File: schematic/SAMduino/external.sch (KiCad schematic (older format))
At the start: 16 parts, among them IC4 SST26VF064B-104V_SM, IC5 MCP2221-I_SL, IC6 MCP2542FD-E_SN, J5 Conn_01x02, J6 Conn_01x02

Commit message: Specialty pins wired
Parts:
- removed JP1: SolderJumper_2_Bridged, symbol Jumper:SolderJumper_2_Bridged
- added R?: 100k, symbol Device:R
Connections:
- net labels added: NRST, QCS, QIO0, QIO1, QIO2, QIO3, QSCK, URXD0, UTXD0
- net labels removed: MCLR, U2RX, U2TX
- wire segments 50 -> 57
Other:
- moved on the sheet: C24
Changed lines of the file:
@@
 	4800 4500 4050 4500
 Text GLabel 1800 4600 0    50   Input ~ 0
-MCLR
+NRST
 Text GLabel 1800 4700 0    50   Input ~ 0
-U2RX
+URXD0
 Text GLabel 1800 4800 0    50   Input ~ 0
-U2TX
+UTXD0
 Wire Wire Line
 	1800 4700 2950 4700
@@
 L power:GND #PWR028
 U 1 1 616BDAE8
-P 3600 1600
-F 0 "#PWR028" H 3600 1350 50  0001 C CNN
-F 1 "GND" H 3605 1427 50  0000 C CNN
-F 2 "" H 3600 1600 50  0001 C CNN
-F 3 "" H 3600 1600 50  0001 C CNN
-	1    3600 1600
+P 3800 1600
+F 0 "#PWR028" H 3800 1350 50  0001 C CNN
+F 1 "GND" H 3805 1427 50  0000 C CNN
+F 2 "" H 3800 1600 50  0001 C CNN
+F 3 "" H 3800 1600 50  0001 C CNN
+	1    3800 1600
 	1    0    0    -1
 $EndComp
@@
 L Device:C C24
 U 1 1 616BE1BB
-P 3300 1600
-F 0 "C24" H 3415 1646 50  0000 L CNN
-F 1 "100n" H 3415 1555 50  0000 L CNN
-F 2 "" H 3338 1450 50  0001 C CNN
-F 3 "~" H 3300 1600 50  0001 C CNN
-	1    3300 1600
+P 3500 1600
+F 0 "C24" V 3250 1500 50  0000 L CNN
+F 1 "100n" V 3350 1500 50  0000 L CNN
+F 2 "" H 3538 1450 50  0001 C CNN
+F 3 "~" H 3500 1600 50  0001 C CNN
+	1    3500 1600
 	0    1    1    0
 $EndComp
 Text GLabel 3000 1300 1    50   Input ~ 0
 VCC3V3
-$Comp
-L Jumper:SolderJumper_2_Bridged JP1
-U 1 1 616C3578
-P 2000 4600
-F 0 "JP1" H 2000 4713 50  0000 C CNN
-F 1 "SolderJumper_2_Bridged" H 2000 4714 50  0001 C CNN
-F 2 "" H 2000 4600 50  0001 C CNN
-F 3 "~" H 2000 4600 50  0001 C CNN
-	1    2000 4600
-	1    0    0    -1
-$EndComp
-Wire Wire Line
-	2150 4600 2950 4600
-Wire Wire Line
-	1850 4600 1800 4600
 Text Notes 7900 3000 0    50   ~ 0
 CAN Transceiver
@@
 	2900 1600 3000 1600
 Wire Wire Line
-	3450 1600 3600 1600
+	3650 1600 3800 1600
 Wire Wire Line
 	3000 1300 3000 1600
+Text GLabel 3050 1800 2    50   Input ~ 0
+QSCK
+Text GLabel 3050 1900 2    50   Input ~ 0
+QIO0
+Text GLabel 1150 1700 0    50   Input ~ 0
+QIO1
+Text GLabel 1150 1800 0    50   Input ~ 0
+QIO2
+Text GLabel 3050 1700 2    50   Input ~ 0
+QIO3
+Text GLabel 1150 1600 0    50   Input ~ 0
+QCS
+Wire Wire Line
+	3000 1600 3350 1600
 Connection ~ 3000 1600
 Wire Wire Line
-	3000 1600 3150 1600
+	3050 1700 2900 1700
+Wire Wire Line
+	3050 1800 2900 1800
+Wire Wire Line
+	3050 1900 2900 1900
+Wire Wire Line
+	1150 1800 1300 1800
+Wire Wire Line
+	1150 1700 1300 1700
+Wire Wire Line
+	1150 1600 1300 1600
+$Comp
+L Device:R R?
+U 1 1 6163C603
+P 1300 1250
+F 0 "R?" H 1370 1296 50  0000 L CNN
+F 1 "100k" H 1370 1205 50  0000 L CNN
+F 2 "" V 1230 1250 50  0001 C CNN
+F 3 "~" H 1300 1250 50  0001 C CNN
+	1    1300 1250
+	1    0    0    -1
+$EndComp
+Text GLabel 1300 1000 1    50   Input ~ 0
+VCC3V3
+Wire Wire Line
+	1300 1400 1300 1600
+Connection ~ 1300 1600
+Wire Wire Line
+	1300 1100 1300 1000
+Wire Wire Line
+	1800 4600 2950 4600
 $EndSCHEMATC

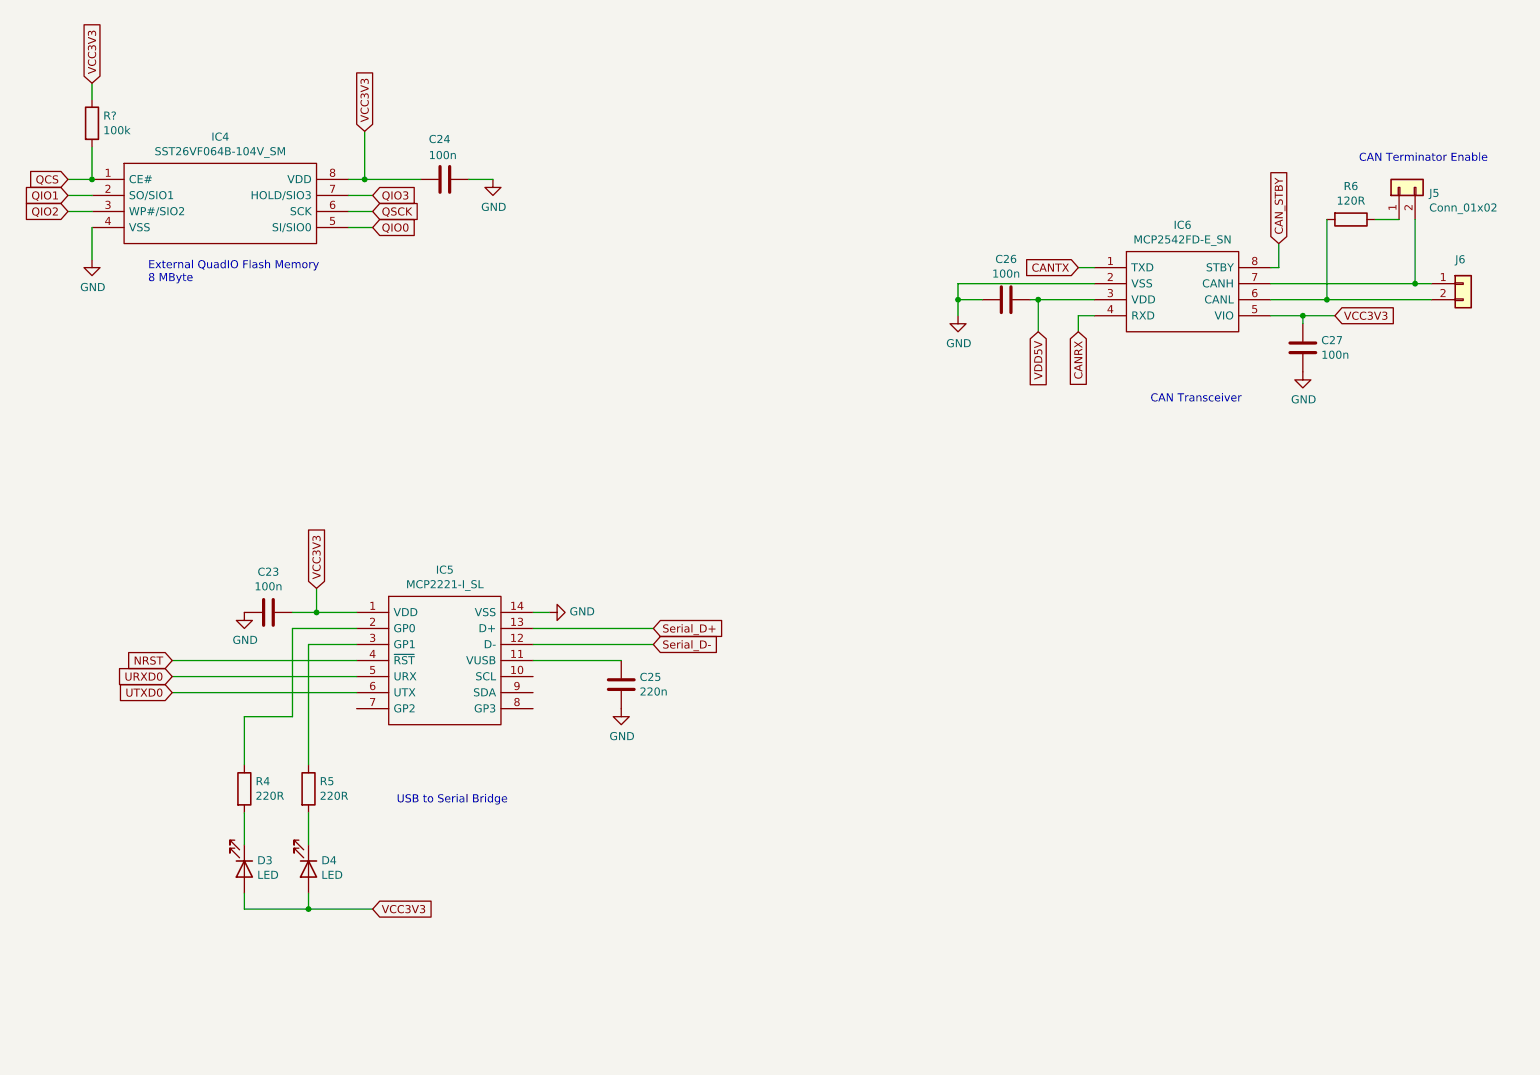
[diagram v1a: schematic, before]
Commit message: All pins connected
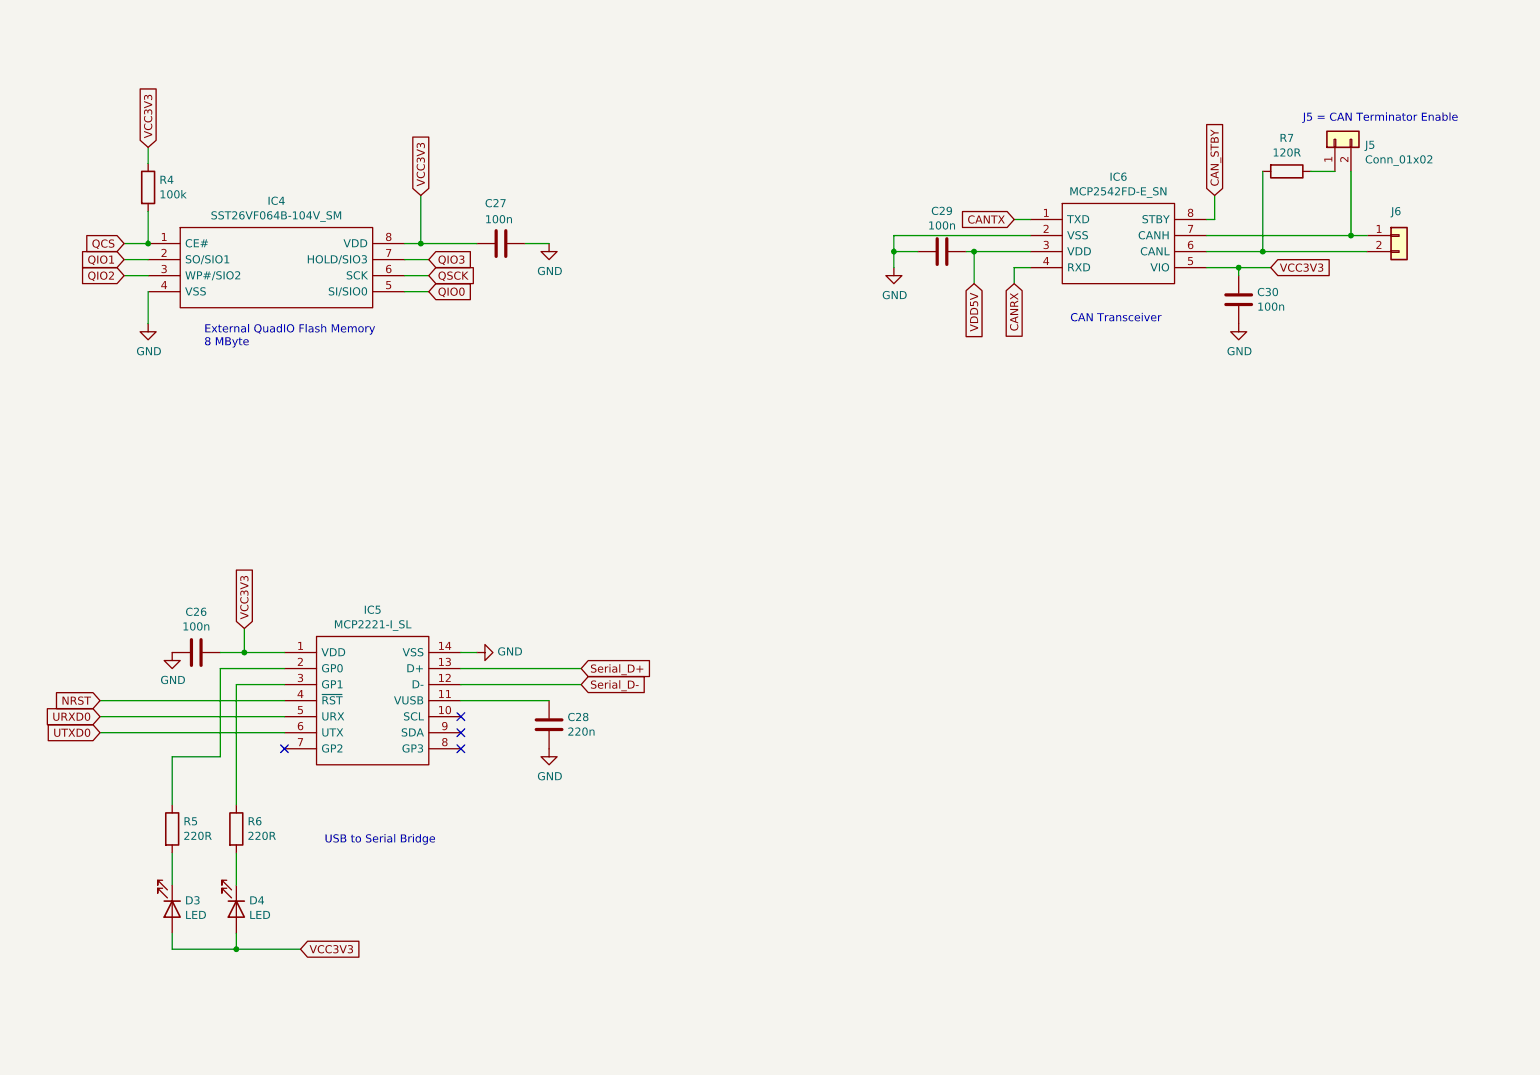
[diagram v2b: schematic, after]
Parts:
- gave numbers to parts that had none: 1
- renumbered C23 to C26, C24 to C27, C25 to C28, C26 to C29, C27 to C30, R4 to R5, R5 to R6, R6 to R7
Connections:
- no-connect marks 0 -> 4
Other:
- note added: "J5 = CAN Terminator Enable"
- note removed: "CAN Terminator Enable"
- moved on the sheet: C26, C27, C28, C29, C30, D3, D4, IC4, IC5, IC6, J5, J6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

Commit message: Schematic with footprints
Some footprints need to be verified with actual components
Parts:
- removed J6: Conn_01x02, symbol Connector_Generic:Conn_01x02
- added J6: Screw_Terminal_01x02, SamacSys_Parts:1725656, symbol Connector:Screw_Terminal_01x02
- C26, C27, C28, C29, C30: footprint (none) -> Capacitor_SMD:C_0603_1608Metric
- D3: value LED -> Green; footprint (none) -> LED_SMD:LED_0603_1608Metric
- D4: value LED -> Yellow; footprint (none) -> LED_SMD:LED_0603_1608Metric
- IC4: footprint SOIC127P794X203-8N -> SamacSys_Parts:SOIC127P794X203-8N
- IC5: footprint SOIC127P600X175-14N -> SamacSys_Parts:SOIC127P600X175-14N
- IC6: footprint SOIC127P600X175-8N -> SamacSys_Parts:SOIC127P600X175-8N
- J5: footprint (none) -> Connector_PinHeader_2.54mm:PinHeader_1x02_P2.54mm_Vertical
- R4, R5, R6: footprint (none) -> Resistor_SMD:R_0603_1608Metric
- R7: footprint (none) -> Resistor_SMD:R_0805_2012Metric
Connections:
- net URXD0: now also IC5.6 (UTX); no longer IC5.5 (URX)
- net UTXD0: now also IC5.5 (URX); no longer IC5.6 (UTX)
- net VCC3V3: now also C28.1, IC5.11 (VUSB)
- net at IC6.6 (CANL), R7.2: now also J6.2 (Pin_2)
- net at IC6.7 (CANH), J5.2 (Pin_2): now also J6.1 (Pin_1)
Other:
- note added: "Is this needed? or 100n instead?"
- note added: "MCU Rx\nindicator"
- note added: "MCU Tx\nindicator"
- moved on the sheet: C28
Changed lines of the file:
@@
 F 0 "IC6" H 7700 2115 50  0000 C CNN
 F 1 "MCP2542FD-E_SN" H 7700 2024 50  0000 C CNN
-F 2 "SOIC127P600X175-8N" H 8100 1950 50  0001 L CNN
+F 2 "SamacSys_Parts:SOIC127P600X175-8N" H 8100 1950 50  0001 L CNN
 F 3 "" H 8100 1850 50  0001 L CNN
 F 4 "Microchip MCP2542FD-E/SN, CAN Transceiver 8Mbit/s 1-Channel CAN, ISO 11898-2, ISO 11898-5, ISO/DIS11898-2, 8-Pin SOIC" H 8100 1750 50  0001 L CNN "Description"
@@
 F 0 "IC5" H 3050 4815 50  0000 C CNN
 F 1 "MCP2221-I_SL" H 3050 4724 50  0000 C CNN
-F 2 "SOIC127P600X175-14N" H 3450 4650 50  0001 L CNN
+F 2 "SamacSys_Parts:SOIC127P600X175-14N" H 3450 4650 50  0001 L CNN
 F 3 "" H 3450 4550 50  0001 L CNN
 F 4 "USB 2.0 to I2C/UART Converter GPIO SO14 Microchip MCP2221-I/SL, USB Converter, USB 2.0 at 12Mbit/s, 3  5.5 V, 14-Pin SOIC" H 3450 4450 50  0001 L CNN "Description"
@@
 F 0 "IC4" H 2450 2265 50  0000 C CNN
 F 1 "SST26VF064B-104V_SM" H 2450 2174 50  0000 C CNN
-F 2 "SOIC127P794X203-8N" H 3100 2100 50  0001 L CNN
+F 2 "SamacSys_Parts:SOIC127P794X203-8N" H 3100 2100 50  0001 L CNN
 F 3 "https://componentsearchengine.com/Datasheets/2/SST26VF064B-104V_SM.pdf" H 3100 2000 50  0001 L CNN
 F 4 "NOR Flash 64Mbit SPI/SQI Flash 2.3V-3.6V, 105C" H 3100 1900 50  0001 L CNN "Description"
@@
 F 0 "C30" H 8565 2396 50  0000 L CNN
 F 1 "100n" H 8565 2305 50  0000 L CNN
-F 2 "" H 8488 2200 50  0001 C CNN
+F 2 "Capacitor_SMD:C_0603_1608Metric" H 8488 2200 50  0001 C CNN
 F 3 "~" H 8450 2350 50  0001 C CNN
 	1    8450 2350
@@
 F 0 "C29" V 6852 2050 50  0000 C CNN
 F 1 "100n" V 6761 2050 50  0000 C CNN
-F 2 "" H 6638 1900 50  0001 C CNN
+F 2 "Capacitor_SMD:C_0603_1608Metric" H 6638 1900 50  0001 C CNN
 F 3 "~" H 6600 2050 50  0001 C CNN
 	1    6600 2050
 	0    -1   -1   0
-$EndComp
-$Comp
-L Connector_Generic:Conn_01x02 J6
-U 1 1 616A3773
-P 9450 1950
-F 0 "J6" H 9400 2100 50  0000 L CNN
-F 1 "Conn_01x02" H 9530 1851 50  0001 L CNN
-F 2 "" H 9450 1950 50  0001 C CNN
-F 3 "~" H 9450 1950 50  0001 C CNN
-	1    9450 1950
-	1    0    0    -1
 $EndComp
 $Comp
@@
 P 9050 1350
 F 0 "J5" V 9014 1162 50  0000 R CNN
-F 1 "Conn_01x02" V 8923 1162 50  0000 R CNN
-F 2 "" H 9050 1350 50  0001 C CNN
+F 1 "Conn_01x02" V 8923 1162 50  0001 R CNN
+F 2 "Connector_PinHeader_2.54mm:PinHeader_1x02_P2.54mm_Vertical" H 9050 1350 50  0001 C CNN
 F 3 "~" H 9050 1350 50  0001 C CNN
 	1    9050 1350
@@
 F 0 "R7" V 8543 1550 50  0000 C CNN
 F 1 "120R" V 8634 1550 50  0000 C CNN
-F 2 "" V 8680 1550 50  0001 C CNN
+F 2 "Resistor_SMD:R_0805_2012Metric" V 8680 1550 50  0001 C CNN
 F 3 "~" H 8750 1550 50  0001 C CNN
 	1    8750 1550
@@
 L Device:C C28
 U 1 1 616AABD0
-P 4150 5000
-F 0 "C28" H 4265 5046 50  0000 L CNN
-F 1 "220n" H 4265 4955 50  0000 L CNN
-F 2 "" H 4188 4850 50  0001 C CNN
-F 3 "~" H 4150 5000 50  0001 C CNN
-	1    4150 5000
+P 4150 5300
+F 0 "C28" H 4265 5346 50  0000 L CNN
+F 1 "220n" H 4265 5255 50  0000 L CNN
+F 2 "Capacitor_SMD:C_0603_1608Metric" H 4188 5150 50  0001 C CNN
+F 3 "~" H 4150 5300 50  0001 C CNN
+	1    4150 5300
 	1    0    0    -1
 $EndComp
@@
 F 0 "C26" V 1698 4550 50  0000 C CNN
 F 1 "100n" V 1789 4550 50  0000 C CNN
-F 2 "" H 1988 4400 50  0001 C CNN
+F 2 "Capacitor_SMD:C_0603_1608Metric" H 1988 4400 50  0001 C CNN
 F 3 "~" H 1950 4550 50  0001 C CNN
 	1    1950 4550
@@
 F 0 "R5" H 1870 5696 50  0000 L CNN
 F 1 "220R" H 1870 5605 50  0000 L CNN
-F 2 "" V 1730 5650 50  0001 C CNN
+F 2 "Resistor_SMD:R_0603_1608Metric" V 1730 5650 50  0001 C CNN
 F 3 "~" H 1800 5650 50  0001 C CNN
 	1    1800 5650
@@
 F 0 "R6" H 2270 5696 50  0000 L CNN
 F 1 "220R" H 2270 5605 50  0000 L CNN
-F 2 "" V 2130 5650 50  0001 C CNN
+F 2 "Resistor_SMD:R_0603_1608Metric" V 2130 5650 50  0001 C CNN
 F 3 "~" H 2200 5650 50  0001 C CNN
 	1    2200 5650
@@
 P 1800 6150
 F 0 "D3" V 1747 6230 50  0000 L CNN
-F 1 "LED" V 1838 6230 50  0000 L CNN
-F 2 "" H 1800 6150 50  0001 C CNN
+F 1 "Green" V 1838 6230 50  0000 L CNN
+F 2 "LED_SMD:LED_0603_1608Metric" H 1800 6150 50  0001 C CNN
 F 3 "~" H 1800 6150 50  0001 C CNN
 	1    1800 6150
@@
 P 2200 6150
 F 0 "D4" V 2147 6230 50  0000 L CNN
-F 1 "LED" V 2238 6230 50  0000 L CNN
-F 2 "" H 2200 6150 50  0001 C CNN
+F 1 "Yellow" V 2238 6230 50  0000 L CNN
+F 2 "LED_SMD:LED_0603_1608Metric" H 2200 6150 50  0001 C CNN
 F 3 "~" H 2200 6150 50  0001 C CNN
 	1    2200 6150
@@
 L power:GND #PWR035
 U 1 1 616B00B3
-P 4150 5150
-F 0 "#PWR035" H 4150 4900 50  0001 C CNN
-F 1 "GND" H 4155 4977 50  0000 C CNN
-F 2 "" H 4150 5150 50  0001 C CNN
-F 3 "" H 4150 5150 50  0001 C CNN
-	1    4150 5150
+P 4150 5450
+F 0 "#PWR035" H 4150 5200 50  0001 C CNN
+F 1 "GND" H 4155 5277 50  0000 C CNN
+F 2 "" H 4150 5450 50  0001 C CNN
+F 3 "" H 4150 5450 50  0001 C CNN
+	1    4150 5450
 	1    0    0    -1
 $EndComp
@@
 Text GLabel 1350 4850 0    50   Input ~ 0
 NRST
+Text GLabel 1350 5050 0    50   Input ~ 0
+URXD0
 Text GLabel 1350 4950 0    50   Input ~ 0
-URXD0
-Text GLabel 1350 5050 0    50   Input ~ 0
 UTXD0
 Wire Wire Line
@@
 F 0 "C27" V 3600 1900 50  0000 L CNN
 F 1 "100n" V 3700 1900 50  0000 L CNN
-F 2 "" H 3888 1850 50  0001 C CNN
+F 2 "Capacitor_SMD:C_0603_1608Metric" H 3888 1850 50  0001 C CNN
 F 3 "~" H 3850 2000 50  0001 C CNN
 	1    3850 2000
@@
 Text Notes 7400 2500 0    50   ~ 0
 CAN Transceiver
-Text Notes 2750 5750 0    50   ~ 0
+Text Notes 2650 5450 0    50   ~ 0
 USB to Serial Bridge
 Text Notes 2000 2650 0    50   ~ 0
@@
 F 0 "R4" H 1720 1696 50  0000 L CNN
 F 1 "100k" H 1720 1605 50  0000 L CNN
-F 2 "" V 1580 1650 50  0001 C CNN
+F 2 "Resistor_SMD:R_0603_1608Metric" V 1580 1650 50  0001 C CNN
 F 3 "~" H 1650 1650 50  0001 C CNN
 	1    1650 1650
@@
 NoConn ~ 3600 5050
 NoConn ~ 3600 5150
+$Comp
+L Connector:Screw_Terminal_01x02 J6
+U 1 1 616DF8B0
+P 9450 1950
+F 0 "J6" H 9530 1896 50  0000 L CNN
+F 1 "Screw_Terminal_01x02" H 9530 1851 50  0001 L CNN
+F 2 "SamacSys_Parts:1725656" H 9450 1950 50  0001 C CNN
+F 3 "~" H 9450 1950 50  0001 C CNN
+	1    9450 1950
+	1    0    0    -1
+$EndComp
+Text GLabel 4250 5000 2    50   Input ~ 0
+VCC3V3
+Wire Wire Line
+	4150 4850 4150 5000
+Wire Wire Line
+	4250 5000 4150 5000
+Connection ~ 4150 5000
+Wire Wire Line
+	4150 5000 4150 5150
+Text Notes 4500 5300 0    50   ~ 0
+Is this needed?  or 100n instead?
+Text Notes 1350 6200 0    50   ~ 0
+MCU Tx\nindicator
+Text Notes 2550 6200 0    50   ~ 0
+MCU Rx\nindicator
 $EndSCHEMATC
